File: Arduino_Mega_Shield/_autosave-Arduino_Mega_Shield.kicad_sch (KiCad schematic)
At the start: 37 parts, among them J1 Conn_01x04, J10 Conn_01x02, J11 Conn_01x02, J12 Conn_01x02, J13 Conn_01x02, J14 Conn_01x02, J15 Motor Driver Connector, J16 Motor Driver Connector, J17 Motor Driver Connector, J18 Motor Driver Connector, J2 Conn_01x04, J3 Conn_01x04, J4 Conn_01x04, J5 Conn_01x02, J6 Conn_01x02, J7 Conn_01x02, J8 Conn_01x02, J9 Conn_01x02

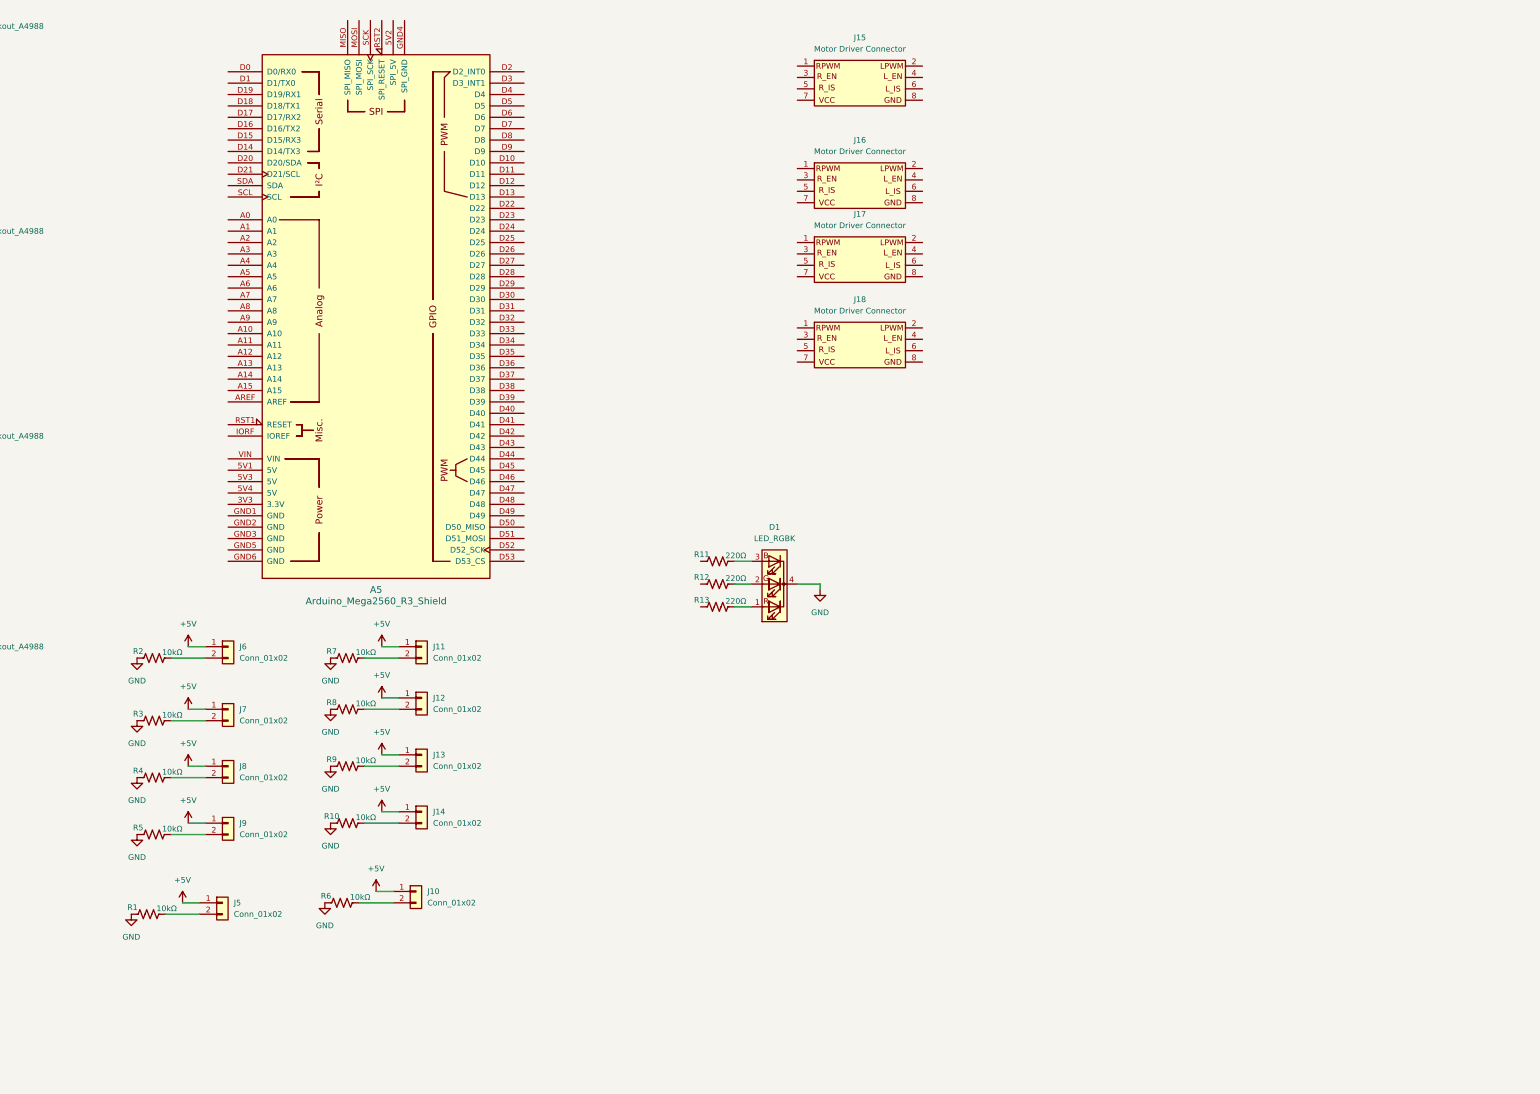
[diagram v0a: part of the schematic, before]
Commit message: Update KiCad PCB (Pololu A4988) and ESP32 code
Replace Arduino Mega shield footprint with a Pololu A4988 breakout footprint and reorganize PCB item positions/annotations (silkscreen, fab, footprint properties, net index adjustments). Add several Arduino_Mega_Shield backup zip files. Also include changes to ESP-32 embedded code (src/main.cpp and src/motor_constants.hpp) — likely motor/driver-related updates to match the hardware footprint changes.
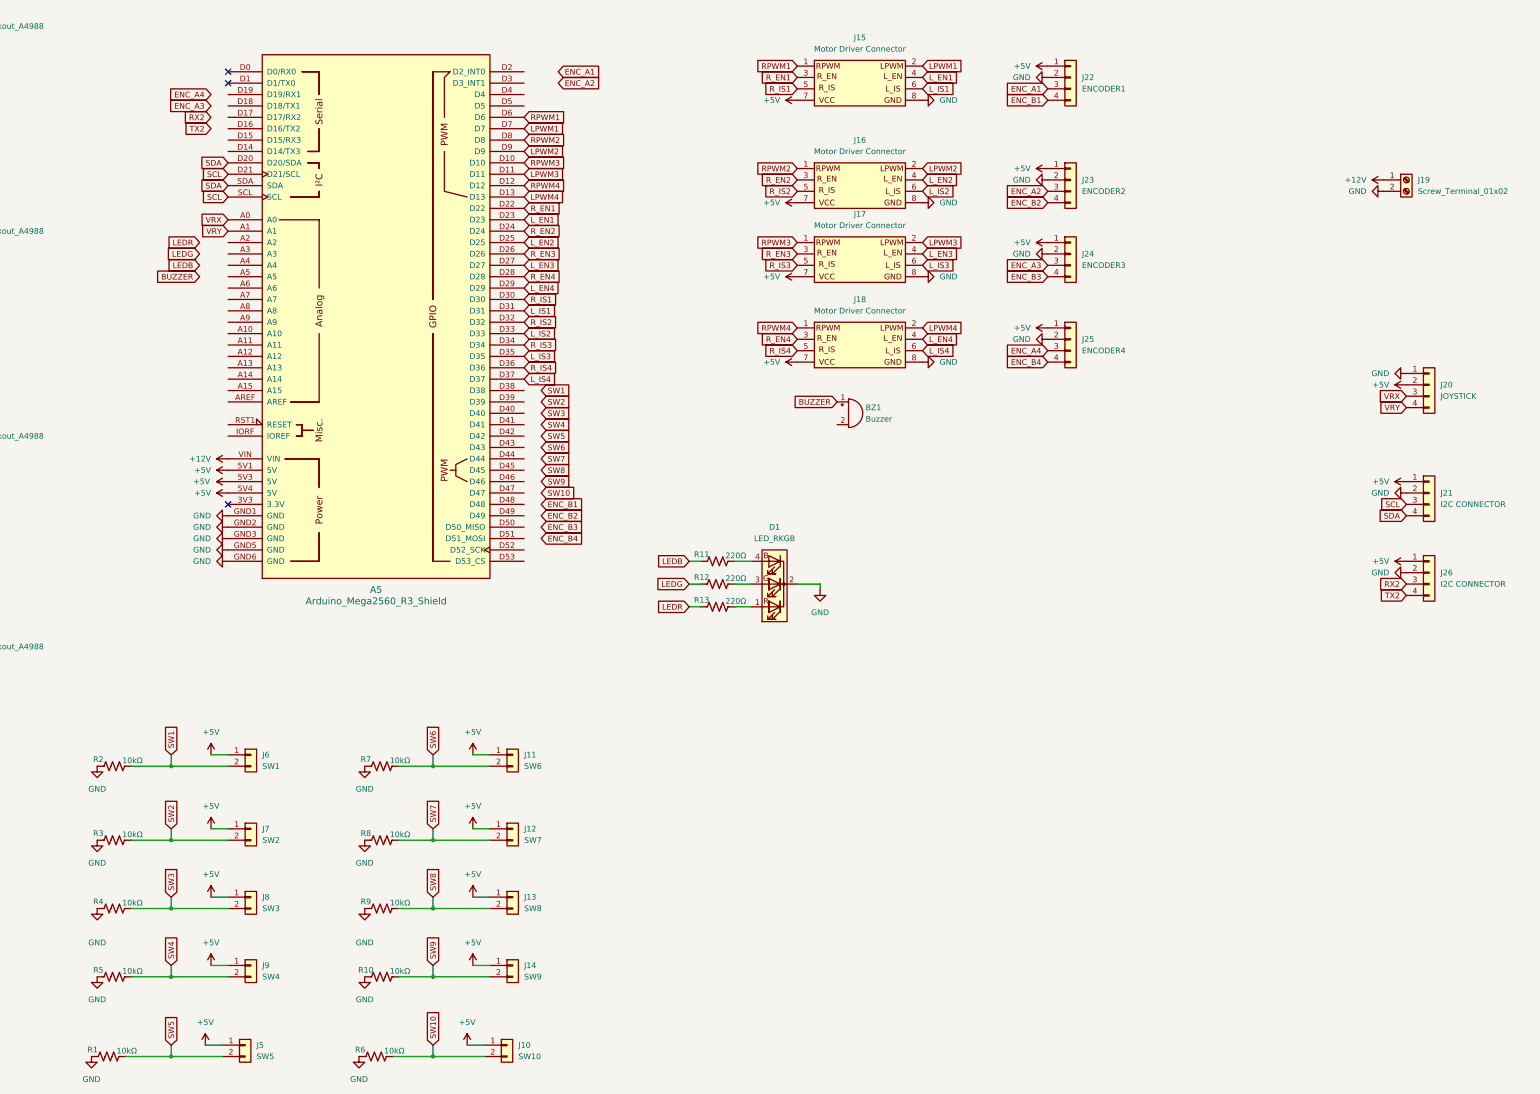
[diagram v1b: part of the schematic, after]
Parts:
- removed D1: LED_RGBK, LED_THT:LED_D5.0mm-4_RGB, symbol Device:LED_RGBK
- added BZ1: Buzzer, Buzzer_Beeper:Buzzer_12x9.5RM7.6, symbol Device:Buzzer
- added D1: LED_RKGB, LED_THT:LED_D5.0mm-4_RGB_Wide_Pins, symbol Device:LED_RKGB
- added J19: Screw_Terminal_01x02, TerminalBlock_RND:TerminalBlock_RND_205-00232_1x02_P5.08mm_Horizontal, symbol Connector:Screw_Terminal_01x02
- added J20: JOYSTICK, Connector_PinHeader_2.54mm:PinHeader_1x04_P2.54mm_Vertical, symbol Connector_Generic:Conn_01x04
- added J21, J26: I2C CONNECTOR, Connector_PinHeader_2.54mm:PinHeader_1x04_P2.54mm_Vertical, symbol Connector_Generic:Conn_01x04
- added J22: ENCODER1, Connector_PinHeader_2.54mm:PinHeader_1x04_P2.54mm_Vertical, symbol Connector_Generic:Conn_01x04
- added J23: ENCODER2, Connector_PinHeader_2.54mm:PinHeader_1x04_P2.54mm_Vertical, symbol Connector_Generic:Conn_01x04
- added J24: ENCODER3, Connector_PinHeader_2.54mm:PinHeader_1x04_P2.54mm_Vertical, symbol Connector_Generic:Conn_01x04
- added J25: ENCODER4, Connector_PinHeader_2.54mm:PinHeader_1x04_P2.54mm_Vertical, symbol Connector_Generic:Conn_01x04
- J10: value Conn_01x02 -> SW10
- J11: value Conn_01x02 -> SW6
- J12: value Conn_01x02 -> SW7
- J13: value Conn_01x02 -> SW8
- J14: value Conn_01x02 -> SW9
- J5: value Conn_01x02 -> SW5
- J6: value Conn_01x02 -> SW1
- J7: value Conn_01x02 -> SW2
- J8: value Conn_01x02 -> SW3
- J9: value Conn_01x02 -> SW4
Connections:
- net +5V: now also A5.5V1 (5V), A5.5V3 (5V), A5.5V4 (5V), J15.7 (Pin_7), J16.7 (Pin_7), J17.7 (Pin_7), J18.7 (Pin_7), J20.2 (Pin_2), J21.1 (Pin_1), J22.1 (Pin_1), J23.1 (Pin_1), J24.1 (Pin_1), J25.1 (Pin_1), J26.1 (Pin_1)
- net GND: now also A5.GND1 (GND), A5.GND2 (GND), A5.GND3 (GND), A5.GND5 (GND), A5.GND6 (GND), J15.8 (Pin_8), J16.8 (Pin_8), J17.8 (Pin_8), J18.8 (Pin_8), D1.2 (K), J19.2 (Pin_2), J20.1 (Pin_1), J21.2 (Pin_2), J22.2 (Pin_2), J23.2 (Pin_2), J24.2 (Pin_2), J25.2 (Pin_2), J26.2 (Pin_2)
- net SW1: now reaches J6.2 (Pin_2), R2.2
- net SW6: now reaches J11.2 (Pin_2), R7.2
- net SW2: now reaches J7.2 (Pin_2), R3.2
- net SW10: now reaches J10.2 (Pin_2), R6.2
- net SW5: now reaches J5.2 (Pin_2), R1.2
- net LEDG: now reaches R12.1
- net at R12.2: now also D1.3 (GA)
- net LEDB: now reaches R11.1
- net at R11.2: now also D1.4 (BA)
- net SW4: now reaches J9.2 (Pin_2), R5.2
- net SW3: now reaches J8.2 (Pin_2), R4.2
- net SW8: now reaches J13.2 (Pin_2), R9.2
- net RPWM1: now reaches J15.1 (Pin_1)
- net RPWM1: now also A5.D6
- net LPWM1: now reaches J15.2 (Pin_2)
- net LPWM1: now also A5.D7
- net R_EN1: now reaches J15.3 (Pin_3)
- net R_EN1: now also A5.D22
- net L_EN1: now reaches J15.4 (Pin_4)
- net L_EN1: now also A5.D23
- net R_IS1: now reaches J15.5 (Pin_5)
- net R_IS1: now also A5.D30
- net L_IS1: now reaches J15.6 (Pin_6)
- net L_IS1: now also A5.D31
- net SW7: now reaches J12.2 (Pin_2), R8.2
- net SW9: now reaches J14.2 (Pin_2), R10.2
- net at R13.2: now also D1.1 (RA)
- net RPWM4: now reaches J18.1 (Pin_1)
- net RPWM4: now also A5.D12
- net LPWM4: now reaches J18.2 (Pin_2)
- net LPWM4: now also A5.D13
- net R_EN4: now reaches J18.3 (Pin_3)
- net R_EN4: now also A5.D28
- net L_EN4: now reaches J18.4 (Pin_4)
- net L_EN4: now also A5.D29
- net R_IS4: now reaches J18.5 (Pin_5)
- net R_IS4: now also A5.D36
- net L_IS4: now reaches J18.6 (Pin_6)
- net L_IS4: now also A5.D37
- net VRX: now reaches A5.A0
- net VRX: now also J20.3 (Pin_3)
- net VRY: now reaches A5.A1
- net VRY: now also J20.4 (Pin_4)
- net RPWM3: now reaches A5.D10
- net RPWM3: now also J17.1 (Pin_1)
- net LPWM3: now reaches A5.D11
- net LPWM3: now also J17.2 (Pin_2)
- net SDA: now reaches A5.D20 (D20/SDA)
- net SDA: now also A5.SDA, J21.4 (Pin_4)
- net SCL: now reaches A5.D21 (D21/SCL)
- net SCL: now also A5.SCL, J21.3 (Pin_3)
- net R_EN2: now reaches A5.D24
- net R_EN2: now also J16.3 (Pin_3)
- net L_EN2: now reaches A5.D25
- net L_EN2: now also J16.4 (Pin_4)
- net R_EN3: now reaches A5.D26
- net R_EN3: now also J17.3 (Pin_3)
- net L_EN3: now reaches A5.D27
- net L_EN3: now also J17.4 (Pin_4)
- net R_IS2: now reaches A5.D32
- net R_IS2: now also J16.5 (Pin_5)
- net L_IS2: now reaches A5.D33
- net L_IS2: now also J16.6 (Pin_6)
- net R_IS3: now reaches A5.D34
- net R_IS3: now also J17.5 (Pin_5)
- net L_IS3: now reaches A5.D35
- net L_IS3: now also J17.6 (Pin_6)
- net RPWM2: now reaches A5.D8
- net RPWM2: now also J16.1 (Pin_1)
- net LPWM2: now reaches A5.D9
- net LPWM2: now also J16.2 (Pin_2)
- net +12V: now reaches A5.VIN
- net +12V: now also J19.1 (Pin_1)
- net LEDR: now reaches R13.1
- new net BUZZER: BZ1.1 (+)
- new net ENC_A1: J22.3 (Pin_3)
- new net ENC_A2: J23.3 (Pin_3)
- new net ENC_A3: J24.3 (Pin_3)
- new net ENC_A4: J25.3 (Pin_3)
- new net ENC_B1: J22.4 (Pin_4)
- new net ENC_B2: J23.4 (Pin_4)
- new net ENC_B3: J24.4 (Pin_4)
- new net ENC_B4: J25.4 (Pin_4)
- new net RX2: J26.3 (Pin_3)
- new net TX2: J26.4 (Pin_4)
- no-connect marks 0 -> 3
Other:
- moved on the sheet: J10, J11, J12, J13, J14, J5, J6, J7, J8, J9, R1, R10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
